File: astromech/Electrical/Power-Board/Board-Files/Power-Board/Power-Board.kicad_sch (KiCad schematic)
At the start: 52 parts, among them Q1 Q_NMOS_DSG, U1 LTC7003

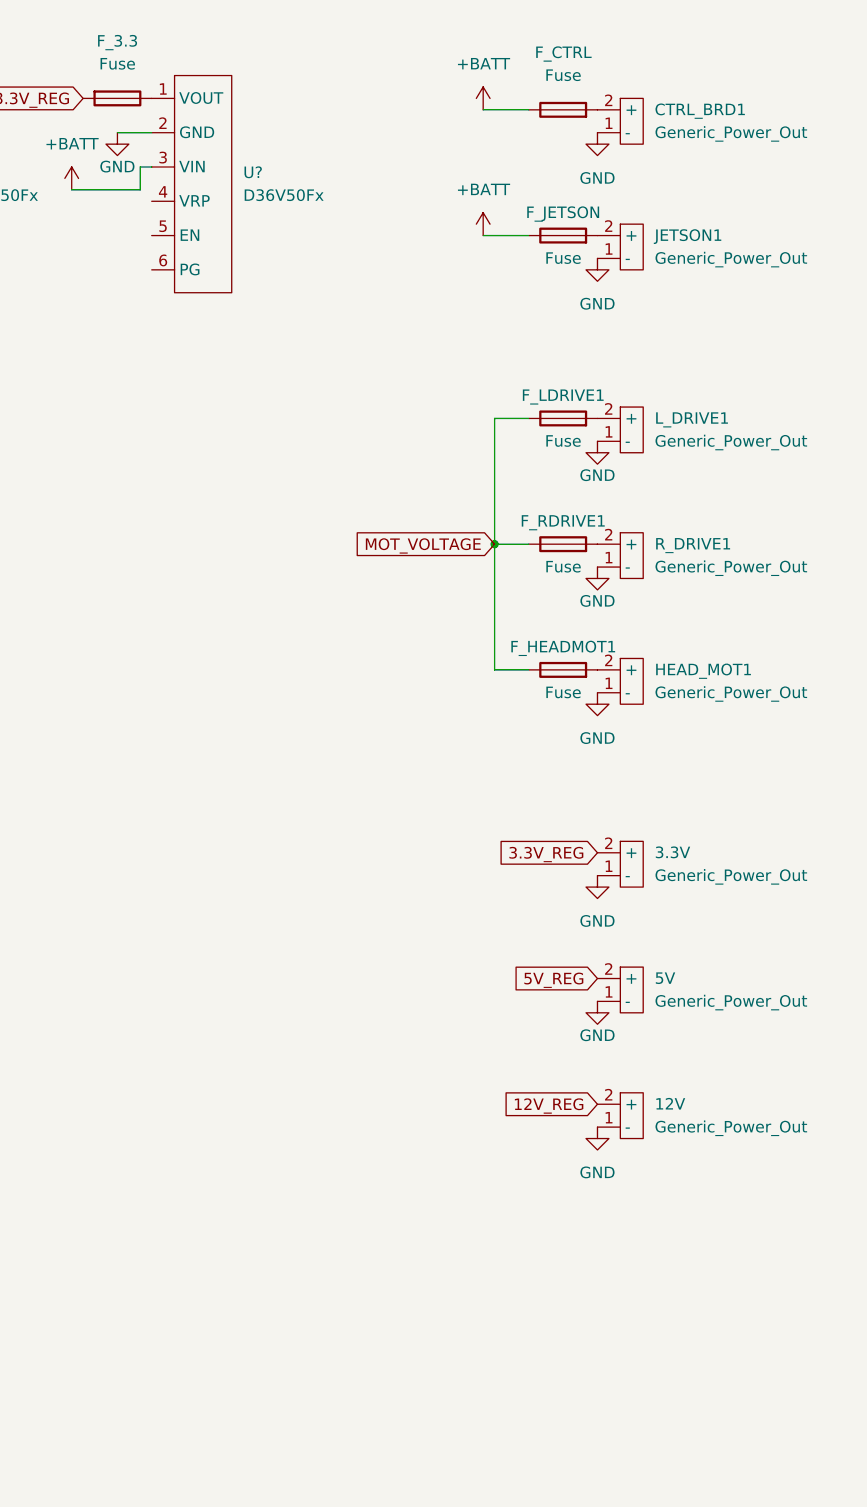
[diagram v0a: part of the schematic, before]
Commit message: expanded regulator outputs to 4 outputs each
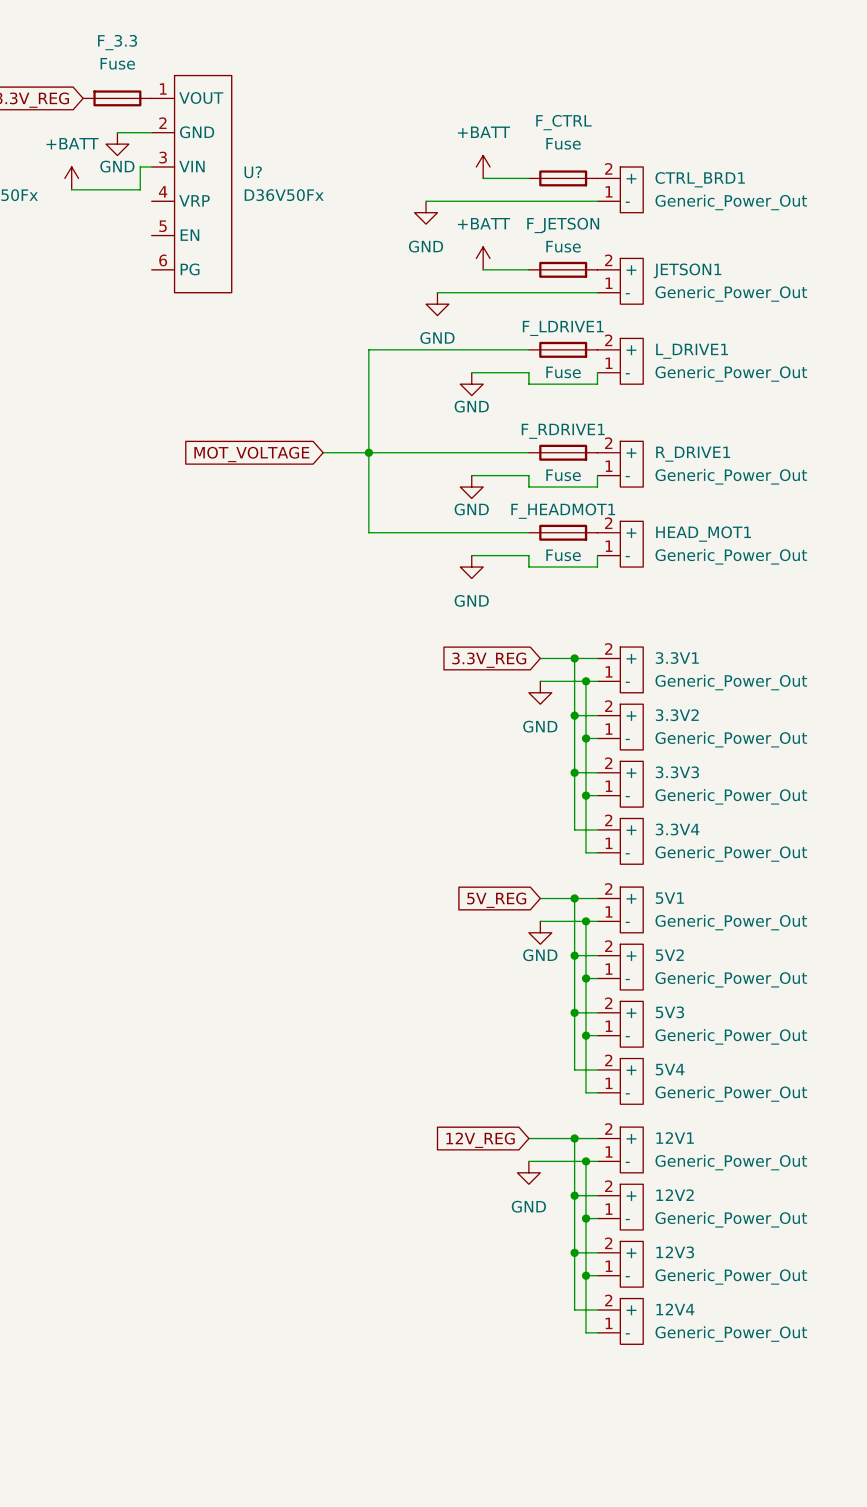
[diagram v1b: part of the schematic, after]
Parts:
- added 12V2, 12V3, 12V4, 3.3V1, 3.3V3, 3.3V4, 5V2, 5V3, 5V4: Generic_Power_Out, symbol astromech-power-board:Generic_Power_Out
- renumbered 12V to 12V1, 3.3V to 3.3V2, 5V to 5V1
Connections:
- net 12V_REG: now also 12V2.2 (+), 12V3.2 (+), 12V4.2 (+)
- net 3.3V_REG: now also 3.3V1.2 (+), 3.3V3.2 (+), 3.3V4.2 (+)
- net 5V_REG: now also 5V2.2 (+), 5V3.2 (+), 5V4.2 (+)
- net GND: now also 12V2.1 (-), 12V3.1 (-), 12V4.1 (-), 3.3V1.1 (-), 3.3V3.1 (-), 3.3V4.1 (-), 5V2.1 (-), 5V3.1 (-), 5V4.1 (-)
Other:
- moved on the sheet: 12V1, 3.3V2, 5V1, CTRL_BRD1, F_CTRL, F_HEADMOT1, F_JETSON, F_LDRIVE1, F_RDRIVE1, HEAD_MOT1, JETSON1, L_DRIVE1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

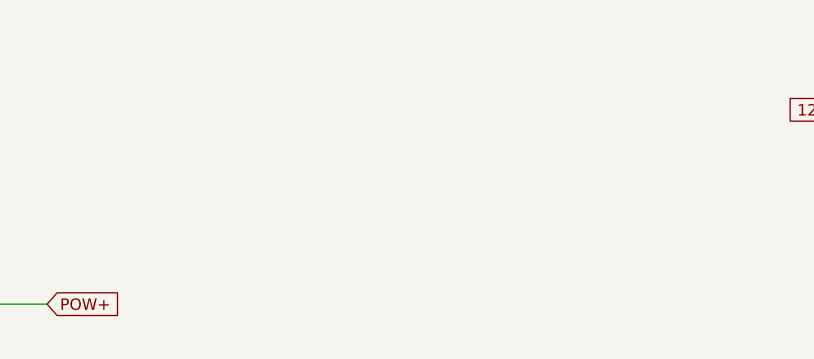
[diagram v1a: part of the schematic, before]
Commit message: Added Level Shifter
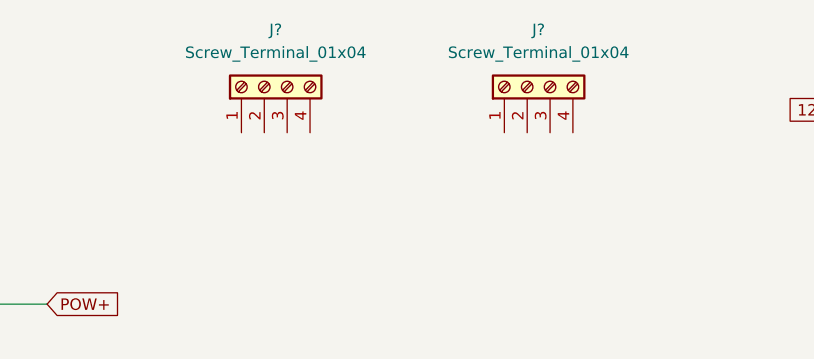
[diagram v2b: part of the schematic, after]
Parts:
- added J? (x2): Screw_Terminal_01x04, symbol Connector:Screw_Terminal_01x04
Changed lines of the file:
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@@
     (pin "2")
+  )
+  (symbol (lib_id "Connector:Screw_Terminal_01x04") (at 99.06 20.32 90) (unit 1)
+    (in_bom yes) (on_board yes) (fields_autoplaced)
+    (property "Reference" "J?" (id 0) (at 100.33 13.97 90))
+    (property "Value" "Screw_Terminal_01x04" (id 1) (at 100.33 16.51 90))
+    (property "Footprint" "" (id 2) (at 99.06 20.32 0)
+      (effects (font (size 1.27 1.27)) hide)
+    )
+    (property "Datasheet" "~" (id 3) (at 99.06 20.32 0)
+      (effects (font (size 1.27 1.27)) hide)
+    )
+    (pin "1")
+    (pin "2")
+    (pin "3")
+    (pin "4")
   )
   (symbol (lib_id "astromech-power-board:D36V50Fx") (at 212.09 30.48 0) (unit 1)
@@
     (pin "2")
   )
+  (symbol (lib_id "Connector:Screw_Terminal_01x04") (at 69.85 20.32 90) (unit 1)
+    (in_bom yes) (on_board yes) (fields_autoplaced)
+    (property "Reference" "J?" (id 0) (at 71.12 13.97 90))
+    (property "Value" "Screw_Terminal_01x04" (id 1) (at 71.12 16.51 90))
+    (property "Footprint" "" (id 2) (at 69.85 20.32 0)
+      (effects (font (size 1.27 1.27)) hide)
+    )
+    (property "Datasheet" "~" (id 3) (at 69.85 20.32 0)
+      (effects (font (size 1.27 1.27)) hide)
+    )
+    (pin "1")
+    (pin "2")
+    (pin "3")
+    (pin "4")
+  )
   (symbol (lib_id "Device:Fuse") (at 173.99 22.86 90) (unit 1)
     (in_bom yes) (on_board yes) (fields_autoplaced)
@@
       (reference "HEAD_MOT1") (unit 1) (value "Generic_Power_Out") (footprint "")
     )
+    (path "/b820aef2-67d9-4b54-8897-e50af9866ca7"
+      (reference "J?") (unit 1) (value "Screw_Terminal_01x04") (footprint "")
+    )
+    (path "/c07046d0-c26a-4bcd-9e92-59b0cb79e848"
+      (reference "J?") (unit 1) (value "Screw_Terminal_01x04") (footprint "")
+    )
     (path "/90e4866f-9ea5-4fc2-a1e2-380f8be15bb6"

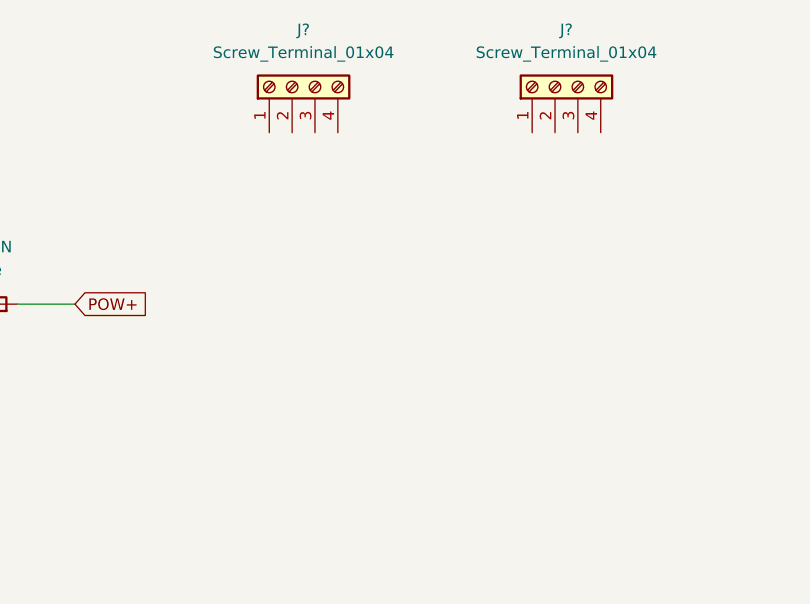
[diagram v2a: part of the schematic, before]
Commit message: Actually added level shifter
Forgot to save schematic in last commit
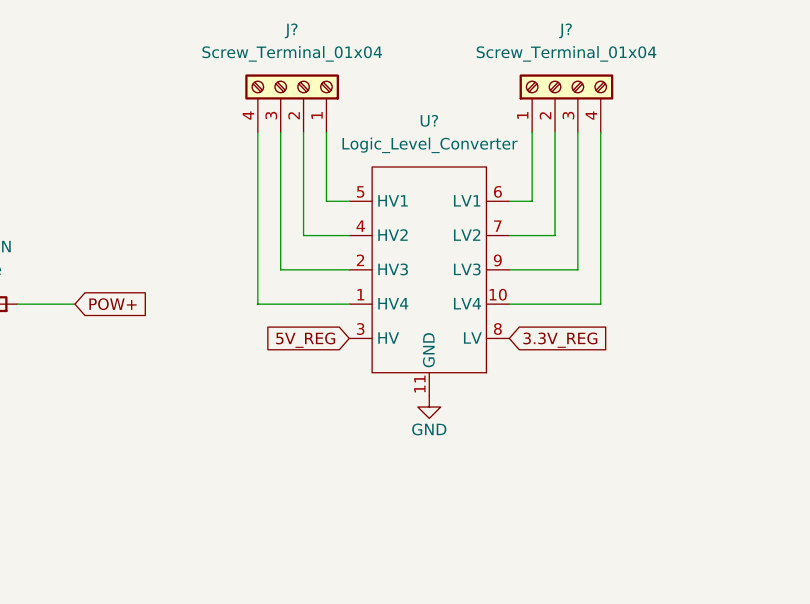
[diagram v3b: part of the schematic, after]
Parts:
- added U?: Logic_Level_Converter, symbol astromech-power-board:Logic_Level_Converter
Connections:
- net 3.3V_REG: now also U?.8 (LV)
- net 5V_REG: now also U?.3 (HV)
- net GND: now also U?.11 (GND)
- net at J?.1 (Pin_1): now also U?.6 (LV1)
- net at J?.2 (Pin_2): now also U?.7 (LV2)
- net at J?.3 (Pin_3): now also U?.9 (LV3)
- net at J?.4 (Pin_4): now also U?.10 (LV4)
- net at J?.1 (Pin_1): now also U?.5 (HV1)
- net at J?.2 (Pin_2): now also U?.4 (HV2)
- net at J?.3 (Pin_3): now also U?.2 (HV3)
- net at J?.4 (Pin_4): now also U?.1 (HV4)
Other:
- moved on the sheet: J?
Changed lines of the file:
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@@
+    (stroke (width 0) (type default) (color 0 0 0 0))
+  )
+  (wire (pts (xy 96.52 25.4) (xy 96.52 33.02))
     (stroke (width 0) (type default) (color 0 0 0 0))
   )
@@
     (stroke (width 0) (type default) (color 0 0 0 0))
   )
+  (wire (pts (xy 96.52 33.02) (xy 93.98 33.02))
+    (stroke (width 0) (type default) (color 0 0 0 0))
+  )
   (wire (pts (xy 259.08 85.09) (xy 256.54 85.09))
     (stroke (width 0) (type default) (color 0 0 0 0))
@@
     (stroke (width 0) (type default) (color 0 0 0 0))
   )
+  (wire (pts (xy 99.06 36.83) (xy 93.98 36.83))
+    (stroke (width 0) (type default) (color 0 0 0 0))
+  )
   (wire (pts (xy 233.68 50.8) (xy 233.68 62.23))
     (stroke (width 0) (type default) (color 0 0 0 0))
@@
     (stroke (width 0) (type default) (color 0 0 0 0))
   )
+  (wire (pts (xy 73.66 25.4) (xy 73.66 33.02))
+    (stroke (width 0) (type default) (color 0 0 0 0))
+  )
   (wire (pts (xy 82.55 177.8) (xy 82.55 170.18))
     (stroke (width 0) (type default) (color 0 0 0 0))
@@
     (stroke (width 0) (type default) (color 0 0 0 0))
   )
+  (wire (pts (xy 68.58 25.4) (xy 68.58 40.64))
+    (stroke (width 0) (type default) (color 0 0 0 0))
+  )
   (wire (pts (xy 50.8 180.34) (xy 50.8 190.5))
     (stroke (width 0) (type default) (color 0 0 0 0))
@@
     (stroke (width 0) (type default) (color 0 0 0 0))
   )
+  (wire (pts (xy 104.14 44.45) (xy 93.98 44.45))
+    (stroke (width 0) (type default) (color 0 0 0 0))
+  )
   (wire (pts (xy 177.8 30.48) (xy 176.53 30.48))
     (stroke (width 0) (type default) (color 0 0 0 0))
@@
     (stroke (width 0) (type default) (color 0 0 0 0))
   )
+  (wire (pts (xy 99.06 25.4) (xy 99.06 36.83))
+    (stroke (width 0) (type default) (color 0 0 0 0))
+  )
   (wire (pts (xy 78.74 161.29) (xy 82.55 161.29))
     (stroke (width 0) (type default) (color 0 0 0 0))
@@
     (stroke (width 0) (type default) (color 0 0 0 0))
   )
+  (wire (pts (xy 101.6 25.4) (xy 101.6 40.64))
+    (stroke (width 0) (type default) (color 0 0 0 0))
+  )
   (wire (pts (xy 25.4 53.34) (xy 26.67 53.34))
     (stroke (width 0) (type default) (color 0 0 0 0))
@@
     (stroke (width 0) (type default) (color 0 0 0 0))
   )
+  (wire (pts (xy 66.04 44.45) (xy 76.2 44.45))
+    (stroke (width 0) (type default) (color 0 0 0 0))
+  )
   (wire (pts (xy 33.02 165.1) (xy 39.37 165.1))
     (stroke (width 0) (type default) (color 0 0 0 0))
@@
     (stroke (width 0) (type default) (color 0 0 0 0))
   )
+  (wire (pts (xy 104.14 25.4) (xy 104.14 44.45))
+    (stroke (width 0) (type default) (color 0 0 0 0))
+  )
   (wire (pts (xy 259.08 138.43) (xy 256.54 138.43))
     (stroke (width 0) (type default) (color 0 0 0 0))
@@
     (stroke (width 0) (type default) (color 0 0 0 0))
   )
+  (wire (pts (xy 101.6 40.64) (xy 93.98 40.64))
+    (stroke (width 0) (type default) (color 0 0 0 0))
+  )
+  (wire (pts (xy 71.12 36.83) (xy 76.2 36.83))
+    (stroke (width 0) (type default) (color 0 0 0 0))
+  )
   (wire (pts (xy 100.33 95.25) (xy 100.33 102.87))
     (stroke (width 0) (type default) (color 0 0 0 0))
@@
     (stroke (width 0) (type default) (color 0 0 0 0))
   )
+  (wire (pts (xy 68.58 40.64) (xy 76.2 40.64))
+    (stroke (width 0) (type default) (color 0 0 0 0))
+  )
   (wire (pts (xy 39.37 106.68) (xy 39.37 113.03))
     (stroke (width 0) (type default) (color 0 0 0 0))
@@
     (stroke (width 0) (type default) (color 0 0 0 0))
   )
+  (wire (pts (xy 71.12 25.4) (xy 71.12 36.83))
+    (stroke (width 0) (type default) (color 0 0 0 0))
+  )
   (wire (pts (xy 80.01 172.72) (xy 80.01 176.53))
     (stroke (width 0) (type default) (color 0 0 0 0))
   )
+  (wire (pts (xy 66.04 25.4) (xy 66.04 44.45))
+    (stroke (width 0) (type default) (color 0 0 0 0))
+  )
   (wire (pts (xy 252.73 87.63) (xy 257.81 87.63))
     (stroke (width 0) (type default) (color 0 0 0 0))
@@
   )
   (wire (pts (xy 45.72 44.45) (xy 39.37 44.45))
+    (stroke (width 0) (type default) (color 0 0 0 0))
+  )
+  (wire (pts (xy 73.66 33.02) (xy 76.2 33.02))
     (stroke (width 0) (type default) (color 0 0 0 0))
   )
@@
     )
   )
+  (global_label "5V_REG" (shape input) (at 76.2 48.26 180) (fields_autoplaced)
+    (effects (font (size 1.27 1.27)) (justify right))
+    (property "Intersheet References" "${INTERSHEET_REFS}" (id 0) (at 66.8321 48.1806 0)
+      (effects (font (size 1.27 1.27)) (justify right) hide)
+    )
+  )
   (global_label "12V_REG" (shape input) (at 49.53 82.55 0) (fields_autoplaced)
     (effects (font (size 1.27 1.27)) (justify left))
     (property "Intersheet References" "${INTERSHEET_REFS}" (id 0) (at 60.1074 82.4706 0)
+      (effects (font (size 1.27 1.27)) (justify left) hide)
+    )
+  )
+  (global_label "3.3V_REG" (shape input) (at 93.98 48.26 0) (fields_autoplaced)
+    (effects (font (size 1.27 1.27)) (justify left))
+    (property "Intersheet References" "${INTERSHEET_REFS}" (id 0) (at 105.1621 48.3394 0)
       (effects (font (size 1.27 1.27)) (justify left) hide)
     )
@@
     (pin "3")
   )
+  (symbol (lib_id "astromech-power-board:Logic_Level_Converter") (at 85.09 53.34 180) (unit 1)
+    (in_bom yes) (on_board yes) (fields_autoplaced)
+    (property "Reference" "U?" (id 0) (at 85.09 24.13 0))
+    (property "Value" "Logic_Level_Converter" (id 1) (at 85.09 26.67 0))
+    (property "Footprint" "" (id 2) (at 85.09 48.26 0)
+      (effects (font (size 1.27 1.27)) hide)
+    )
+    (property "Datasheet" "" (id 3) (at 85.09 48.26 0)
+      (effects (font (size 1.27 1.27)) hide)
+    )
+    (pin "1")
+    (pin "10")
+    (pin "11")
+    (pin "2")
+    (pin "3")
+    (pin "4")
+    (pin "5")
+    (pin "6")
+    (pin "7")
+    (pin "8")
+    (pin "9")
+  )
   (symbol (lib_id "power:GND") (at 245.11 64.77 0) (unit 1)
     (in_bom yes) (on_board yes)
@@
     (pin "1")
     (pin "2")
+  )
+  (symbol (lib_id "power:GND") (at 85.09 54.61 0) (unit 1)
+    (in_bom yes) (on_board yes)
+    (property "Reference" "#PWR?" (id 0) (at 85.09 60.96 0)
+      (effects (font (size 1.27 1.27)) hide)
+    )
+    (property "Value" "GND" (id 1) (at 85.09 58.42 0))
+    (property "Footprint" "" (id 2) (at 85.09 54.61 0)
+      (effects (font (size 1.27 1.27)) hide)
+    )
+    (property "Datasheet" "" (id 3) (at 85.09 54.61 0)
+      (effects (font (size 1.27 1.27)) hide)
+    )
+    (pin "1")
   )
   (symbol (lib_id "power:GND") (at 46.99 184.15 0) (unit 1)
@@
     (pin "2")
   )
-  (symbol (lib_id "Connector:Screw_Terminal_01x04") (at 69.85 20.32 90) (unit 1)
-    (in_bom yes) (on_board yes) (fields_autoplaced)
-    (property "Reference" "J?" (id 0) (at 71.12 13.97 90))
-    (property "Value" "Screw_Terminal_01x04" (id 1) (at 71.12 16.51 90))
-    (property "Footprint" "" (id 2) (at 69.85 20.32 0)
-      (effects (font (size 1.27 1.27)) hide)
-    )
-    (property "Datasheet" "~" (id 3) (at 69.85 20.32 0)
+  (symbol (lib_id "Connector:Screw_Terminal_01x04") (at 71.12 20.32 270) (mirror x) (unit 1)
+    (in_bom yes) (on_board yes) (fields_autoplaced)
+    (property "Reference" "J?" (id 0) (at 69.85 13.97 90))
+    (property "Value" "Screw_Terminal_01x04" (id 1) (at 69.85 16.51 90))
+    (property "Footprint" "" (id 2) (at 71.12 20.32 0)
+      (effects (font (size 1.27 1.27)) hide)
+    )
+    (property "Datasheet" "~" (id 3) (at 71.12 20.32 0)
       (effects (font (size 1.27 1.27)) hide)
     )
@@
       (reference "#PWR?") (unit 1) (value "GND") (footprint "")
     )
+    (path "/a4d0ffef-46b2-4598-a83f-816b8e4857c6"
+      (reference "#PWR?") (unit 1) (value "GND") (footprint "")
+    )
     (path "/a65329e5-9e35-4a3a-bca2-4a7680d6f64e"
       (reference "#PWR?") (unit 1) (value "GND") (footprint "")
@@
       (reference "U?") (unit 1) (value "D36V50Fx") (footprint "astromech-footprints:D36V50Fx")
     )
+    (path "/90190d2a-868b-4683-9af5-aeb585080fff"
+      (reference "U?") (unit 1) (value "Logic_Level_Converter") (footprint "")
+    )
     (path "/b90d7ced-c107-4650-987d-af45d91d2eed"

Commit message: switched LTC7003 input to resistive divider
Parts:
- removed R?: 100k, symbol Device:R_US
- added R? (x2): 100k, symbol Device:R_US
- added R?: 220k, symbol Device:R_US
- R?: value 100k -> 220k
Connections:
- net +BATT: now also R?.2
- net GND: now also R?.1, R?.1
- net POW+: now also R?.2
- net at C?.1, R?.1, U?.3 (Vcc): no longer R?.2
- net at R?.1, U?.7 (INP): now also R?.2
- net at U1.7 (INP): now also R?.1, R?.2
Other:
- moved on the sheet: C?, R?

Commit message: added level-shifter footprint
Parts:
- U?: footprint (none) -> astromech-footprints:Sparkfun-Level-shifter
- renumbered R1 to R?, U1 to U?
